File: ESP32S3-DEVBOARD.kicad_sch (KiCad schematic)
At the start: 0 parts

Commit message: Created library for USB_C, ESP32, AND CP2102N, starded to draw schematic
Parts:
- added C1: 100n, symbol Device:C_Small
- added J1: G-Switch_GT-USB-7010ASV, ESP32S3-DEVBOARD:USB_C_Receptacle_G-Switch_GT-USB-7010ASV, symbol ESP32S3-DEVBOARD:USB_C_Receptacle_G-Switch_GT-USB-7010ASV
- added R1, R2: 5k1, symbol Device:R_Small
- added U1: ESP32-S3-WROOM-1, ESP32S3-DEVBOARD:ESP32-S3-WROOM-1, symbol ESP32S3-DEVBOARD:ESP32-S3-WROOM-1
- added U2: CP2102N-A02-GQFN28R, ESP32S3-DEVBOARD:CP2102N-A02-GQFN28R, symbol ESP32S3-DEVBOARD:CP2102N-A02-GQFN28R
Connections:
- new net: U2.29 (GND), U2.3 (GND)
- new net: U1.1 (GND), U1.40 (GND), U1.41 (GND)
- new net +5V: C1.1, J1.A4 (VBUS), J1.A9 (VBUS), J1.B4 (VBUS), J1.B9 (VBUS)
- new net CC1: J1.A5 (CC1), R1.1
- new net CC2: J1.B5 (CC2), R2.1
- new net D_N: J1.A6 (D+), J1.B6 (D+), U2.5 (D-)
- new net D_P: J1.A7 (D-), J1.B7 (D-), U2.4 (D+)
- new net GND: C1.2, J1.A1 (GND), J1.A12 (GND), J1.B1 (GND), J1.B12 (GND), J1.S1 (SHIELD), R1.2, R2.2
- no-connect marks 0 -> 2

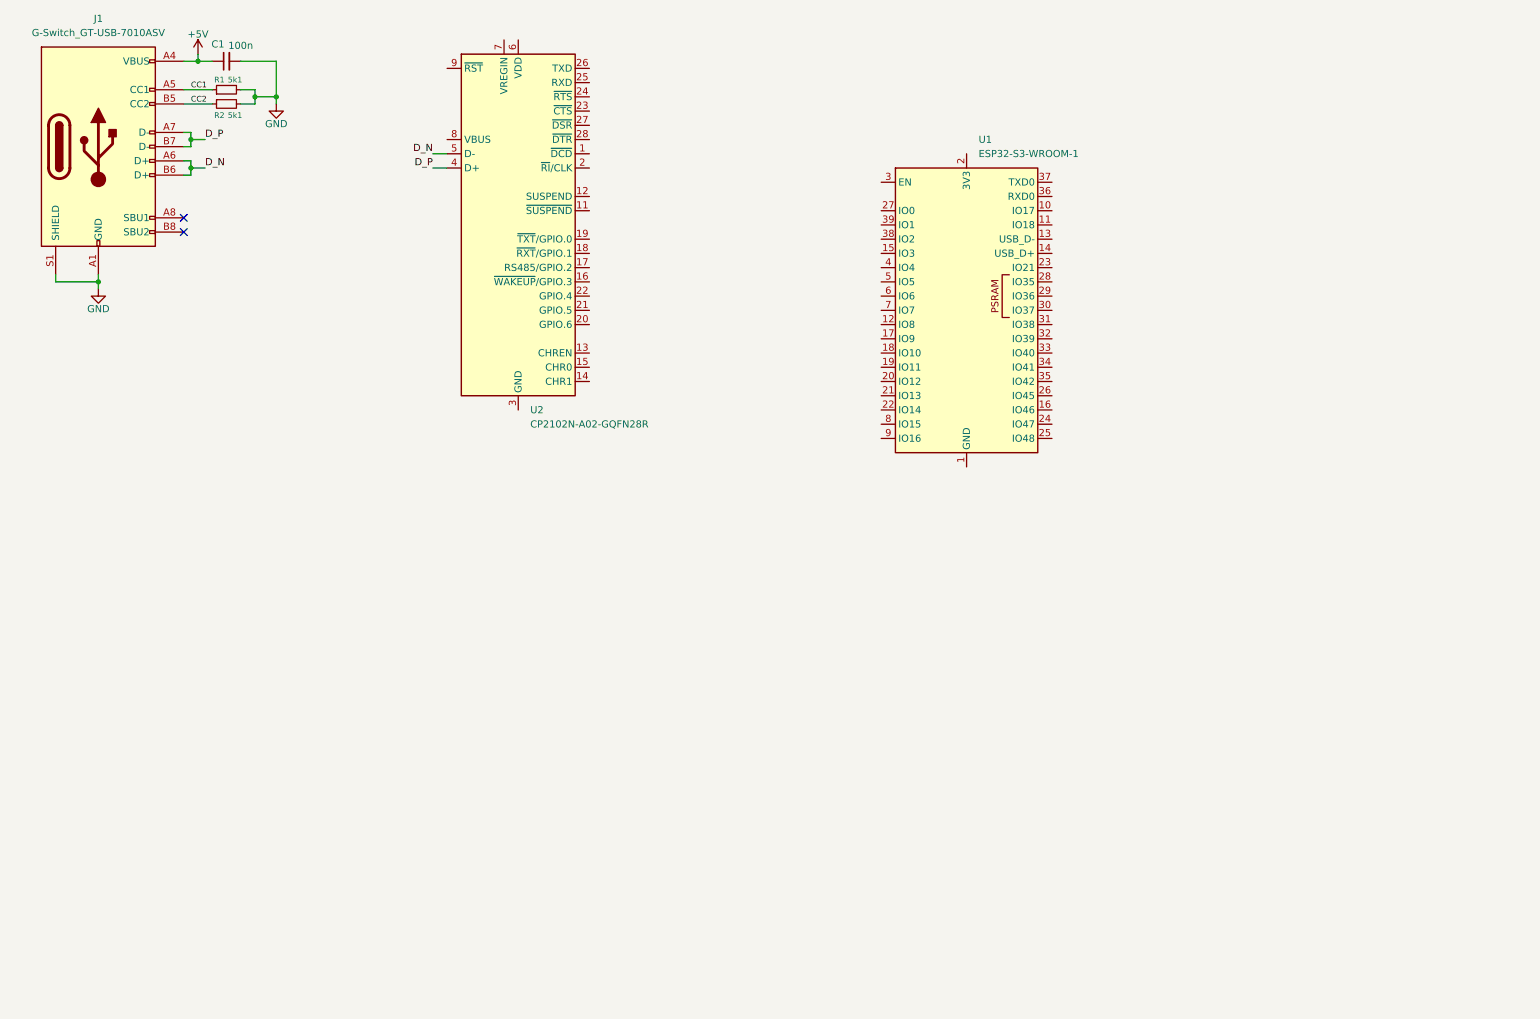
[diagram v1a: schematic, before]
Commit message: Add goldpin, add LDO
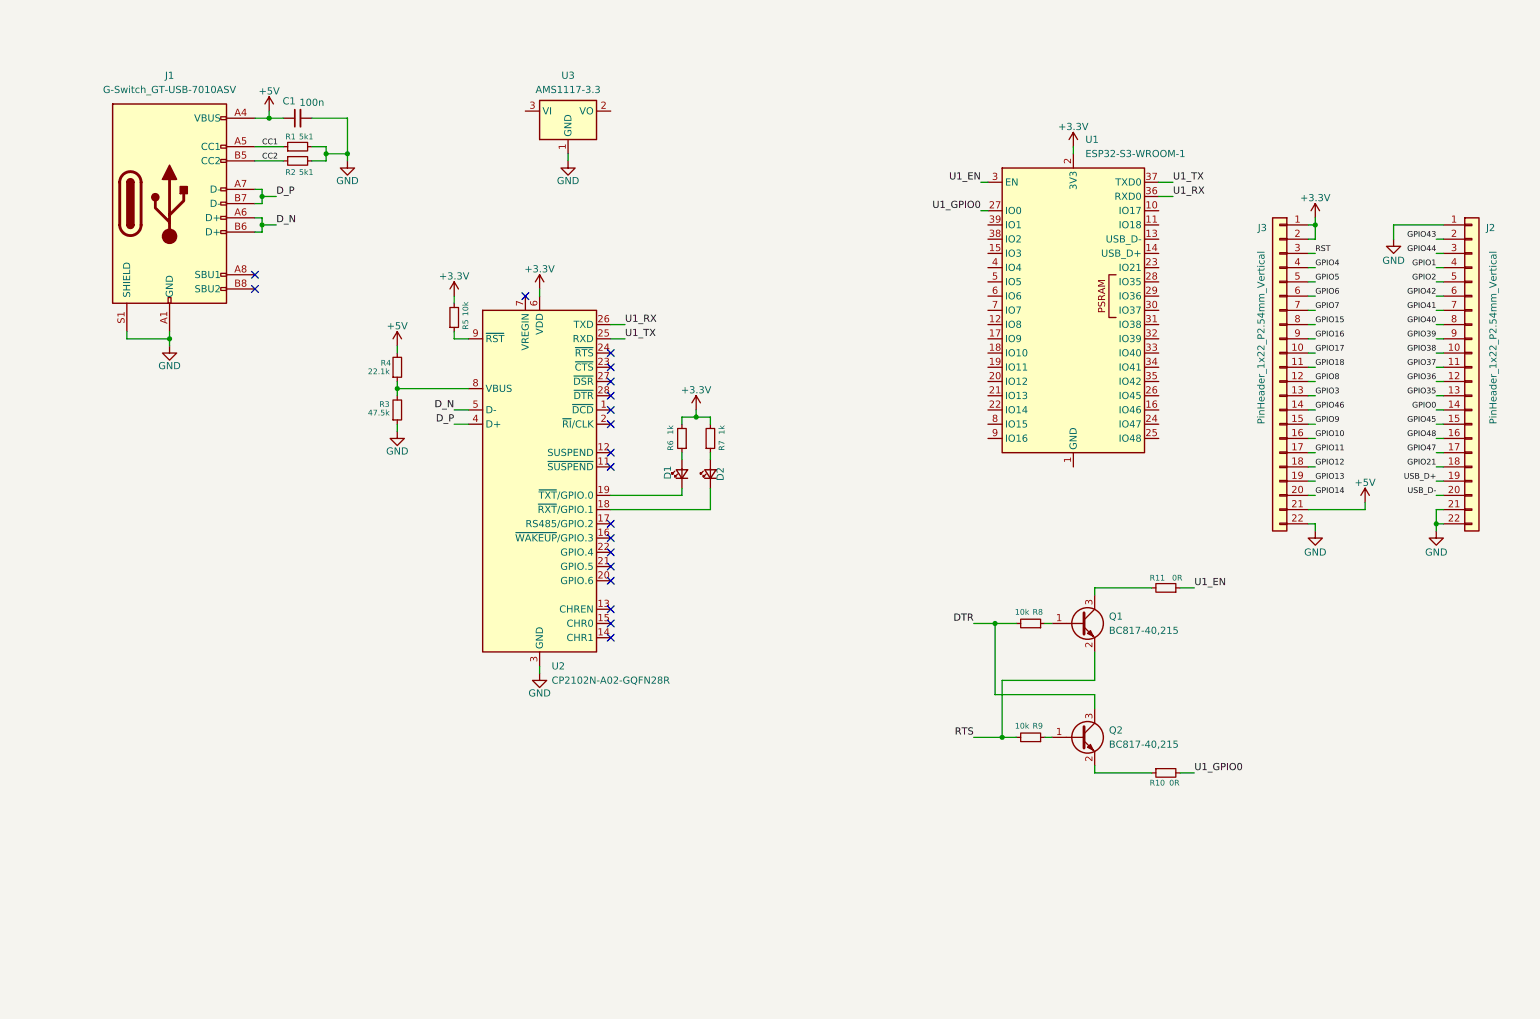
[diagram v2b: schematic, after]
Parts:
- added D1, D2: LED_Small, symbol Device:LED_Small
- added J2, J3: PinHeader_1x22_P2.54mm_Vertical, ESP32S3-DEVBOARD:PinHeader_1x22_P2.54mm_Vertical, symbol ESP32S3-DEVBOARD:PinHeader_1x22_P2.54mm_Vertical
- added Q1, Q2: BC817-40,215, ESP32S3-DEVBOARD:BC817-40,215, symbol ESP32S3-DEVBOARD:BC817-40,215
- added R10, R11: 0R, symbol Device:R_Small
- added R3: 47.5k, symbol Device:R_Small
- added R4: 22.1k, symbol Device:R_Small
- added R5, R8, R9: 10k, symbol Device:R_Small
- added R6, R7: 1k, symbol Device:R_Small
- added U3: AMS1117-3.3, ESP32S3-DEVBOARD:AMS1117-3.3, symbol ESP32S3-DEVBOARD:AMS1117-3.3
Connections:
- net +5V: now also J3.21 (Pin_21), R4.2
- net GND: now also U2.29 (GND), U2.3 (GND), J2.1 (Pin_1), J2.21 (Pin_21), J2.22 (Pin_22), J3.22 (Pin_22), R3.1, U3.1 (GND)
- net at U2.18 (~{RXT}/GPIO.1): now also D2.1 (K)
- net at U2.19 (~{TXT}/GPIO.0): now also D1.1 (K)
- net U1_TX: now reaches U2.25 (RXD)
- net U1_TX: now also U1.37 (TXD0)
- net U1_RX: now reaches U2.26 (TXD)
- net U1_RX: now also U1.36 (RXD0)
- net +3.3V: now reaches U2.6 (VDD)
- net +3.3V: now also U1.2 (3V3), J3.1 (Pin_1), J3.2 (Pin_2), R5.2, R6.2, R7.2
- net at U2.8 (VBUS): now also R3.2, R4.1
- net at U2.9 (~{RST}): now also R5.1
- net U1_GPIO0: now reaches U1.27 (IO0)
- net U1_GPIO0: now also R10.2
- net U1_EN: now reaches U1.3 (EN)
- net U1_EN: now also R11.1
- new net: Q1.1 (B), R8.1
- new net: Q1.3 (C), R11.2
- new net: D1.2 (A), R6.1
- new net: Q2.2 (E), R10.1
- new net: D2.2 (A), R7.1
- new net: Q2.1 (B), R9.1
- new net DTR: Q2.3 (C), R8.2
- new net GPIO0: J2.14 (Pin_14)
- new net GPIO1: J2.4 (Pin_4)
- new net GPIO10: J3.16 (Pin_16)
- new net GPIO11: J3.17 (Pin_17)
- new net GPIO12: J3.18 (Pin_18)
- new net GPIO13: J3.19 (Pin_19)
- new net GPIO14: J3.20 (Pin_20)
- new net GPIO15: J3.8 (Pin_8)
- new net GPIO16: J3.9 (Pin_9)
- new net GPIO17: J3.10 (Pin_10)
- new net GPIO18: J3.11 (Pin_11)
- new net GPIO2: J2.5 (Pin_5)
- new net GPIO21: J2.18 (Pin_18)
- new net GPIO3: J3.13 (Pin_13)
- new net GPIO35: J2.13 (Pin_13)
- new net GPIO36: J2.12 (Pin_12)
- new net GPIO37: J2.11 (Pin_11)
- new net GPIO38: J2.10 (Pin_10)
- new net GPIO39: J2.9 (Pin_9)
- new net GPIO4: J3.4 (Pin_4)
- new net GPIO40: J2.8 (Pin_8)
- new net GPIO41: J2.7 (Pin_7)
- new net GPIO42: J2.6 (Pin_6)
- new net GPIO43: J2.2 (Pin_2)
- new net GPIO44: J2.3 (Pin_3)
- new net GPIO45: J2.15 (Pin_15)
- new net GPIO46: J3.14 (Pin_14)
- new net GPIO47: J2.17 (Pin_17)
- new net GPIO48: J2.16 (Pin_16)
- new net GPIO5: J3.5 (Pin_5)
- new net GPIO6: J3.6 (Pin_6)
- new net GPIO7: J3.7 (Pin_7)
- new net GPIO8: J3.12 (Pin_12)
- new net GPIO9: J3.15 (Pin_15)
- new net RST: J3.3 (Pin_3)
- new net RTS: Q1.2 (E), R9.2
- new net USB_D+: J2.19 (Pin_19)
- new net USB_D-: J2.20 (Pin_20)
- no-connect marks 2 -> 19
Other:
- moved on the sheet: C1, J1, R1, R2, U1, U2

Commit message: Add decoupling capacitors
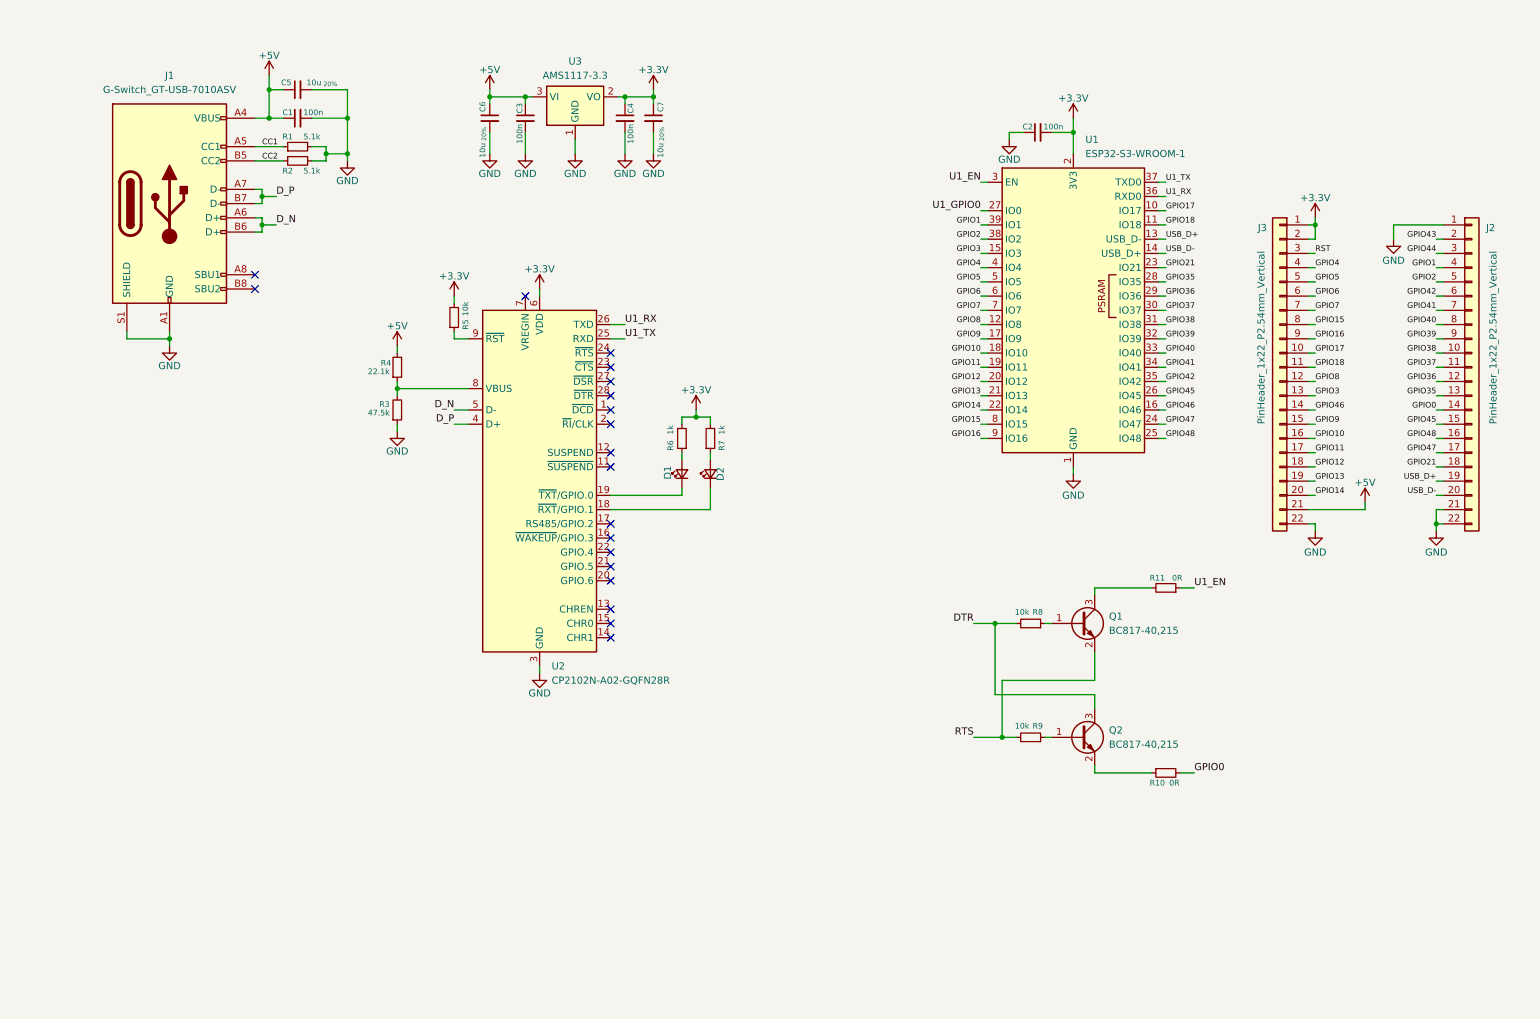
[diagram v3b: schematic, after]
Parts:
- removed C1: 100n, symbol Device:C_Small
- removed R1, R2: 5k1, symbol Device:R_Small
- added C1, C2, C3, C4: 100n, ESP32S3-DEVBOARD:C_0402_1005Metric, symbol ESP32S3-DEVBOARD:CL05B104KO5NNNC
- added C5, C6, C7: 10u_{ 20%}, ESP32S3-DEVBOARD:C_0603_1608Metric, symbol ESP32S3-DEVBOARD:CL10A106MA8NRNC
- added R1, R2: 5.1k, ESP32S3-DEVBOARD:R_0402_1005Metric, symbol ESP32S3-DEVBOARD:0402WGF5101TCE
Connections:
- net +3.3V: now also U3.2 (VO), C2.2, C4.1, C7.1
- net +5V: now also U3.3 (VI), C1.1, C3.1, C5.1, C6.1
- net CC1: now also R1.1
- net CC2: now also R2.1
- net GND: now also U1.1 (GND), U1.40 (GND), U1.41 (GND), C1.2, C2.1, C3.2, C4.2, C5.2, C6.2, C7.2, R1.2, R2.2
- net GPIO0: now also R10.2
- net GPIO1: now also U1.39 (IO1)
- net GPIO10: now also U1.18 (IO10)
- net GPIO11: now also U1.19 (IO11)
- net GPIO12: now also U1.20 (IO12)
- net GPIO13: now also U1.21 (IO13)
- net GPIO14: now also U1.22 (IO14)
- net GPIO15: now also U1.8 (IO15)
- net GPIO16: now also U1.9 (IO16)
- net GPIO17: now also U1.10 (IO17)
- net GPIO18: now also U1.11 (IO18)
- net GPIO2: now also U1.38 (IO2)
- net GPIO21: now also U1.23 (IO21)
- net GPIO3: now also U1.15 (IO3)
- net GPIO35: now also U1.28 (IO35)
- net GPIO36: now also U1.29 (IO36)
- net GPIO37: now also U1.30 (IO37)
- net GPIO38: now also U1.31 (IO38)
- net GPIO39: now also U1.32 (IO39)
- net GPIO4: now also U1.4 (IO4)
- net GPIO40: now also U1.33 (IO40)
- net GPIO41: now also U1.34 (IO41)
- net GPIO42: now also U1.35 (IO42)
- net GPIO45: now also U1.26 (IO45)
- net GPIO46: now also U1.16 (IO46)
- net GPIO47: now also U1.24 (IO47)
- net GPIO48: now also U1.25 (IO48)
- net GPIO5: now also U1.5 (IO5)
- net GPIO6: now also U1.6 (IO6)
- net GPIO7: now also U1.7 (IO7)
- net GPIO8: now also U1.12 (IO8)
- net GPIO9: now also U1.17 (IO9)
- net U1_GPIO0: no longer R10.2
- net USB_D+: now also U1.13 (USB_D-)
- net USB_D-: now also U1.14 (USB_D+)
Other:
- moved on the sheet: U3

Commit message: Add two resisotrs to library
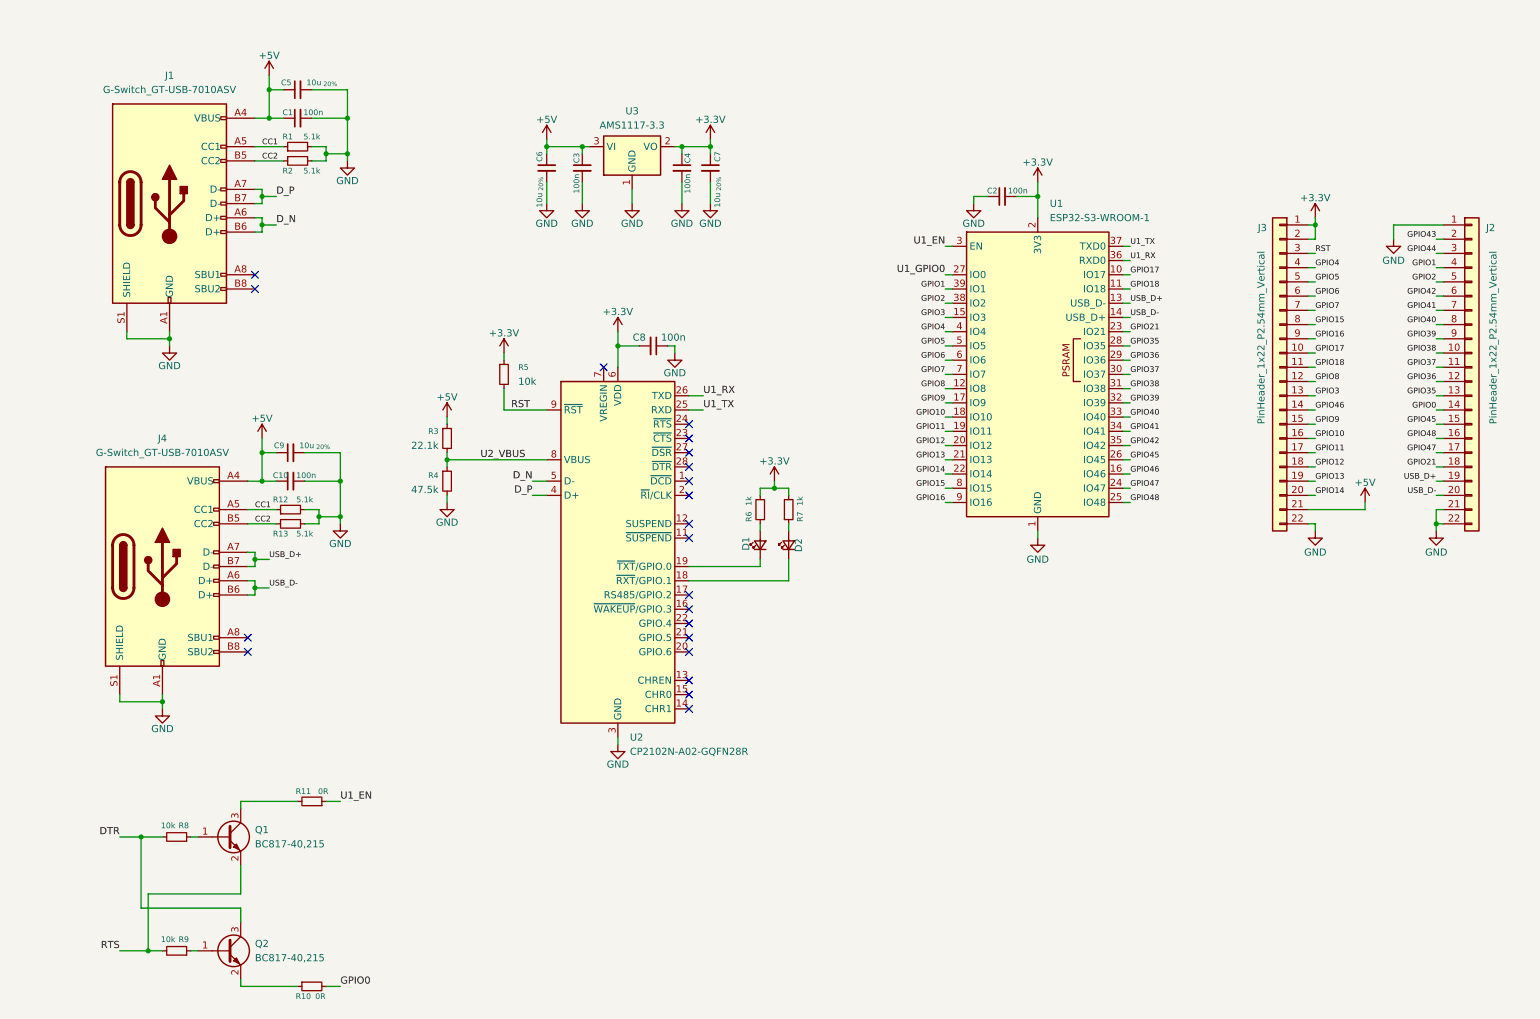
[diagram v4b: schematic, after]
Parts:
- removed R3: 47.5k, symbol Device:R_Small
- removed R4: 22.1k, symbol Device:R_Small
- removed R5, R8: 10k, symbol Device:R_Small
- added C10, C8: 100n, ESP32S3-DEVBOARD:C_0402_1005Metric, symbol ESP32S3-DEVBOARD:CL05B104KO5NNNC
- added C9: 10u_{ 20%}, ESP32S3-DEVBOARD:C_0603_1608Metric, symbol ESP32S3-DEVBOARD:CL10A106MA8NRNC
- added J4: G-Switch_GT-USB-7010ASV, ESP32S3-DEVBOARD:USB_C_Receptacle_G-Switch_GT-USB-7010ASV, symbol ESP32S3-DEVBOARD:USB_C_Receptacle_G-Switch_GT-USB-7010ASV
- added R12, R13: 5.1k, ESP32S3-DEVBOARD:R_0402_1005Metric, symbol ESP32S3-DEVBOARD:0402WGF5101TCE
- added R3: 22.1k, ESP32S3-DEVBOARD:R_0402_1005Metric, symbol ESP32S3-DEVBOARD:FRC0402F2212TS
- added R4: 47.5k, ESP32S3-DEVBOARD:R_0402_1005Metric, symbol ESP32S3-DEVBOARD:0402WGF4752TCE
- added R5, R8: 10k, ESP32S3-DEVBOARD:R_0402_1005Metric, symbol ESP32S3-DEVBOARD:RC0402FR-0710KL
- R9: footprint (none) -> ESP32S3-DEVBOARD:R_0402_1005Metric; symbol Device:R_Small -> ESP32S3-DEVBOARD:RC0402FR-0710KL; LCSC (none) -> C60490; Mfr. Part #  (none) -> RC0402FR-0710KL
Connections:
- net +3.3V: now also C8.2, R5.1
- net +5V: now also C10.1, C9.1, J4.A4 (VBUS), J4.A9 (VBUS), J4.B4 (VBUS), J4.B9 (VBUS), R3.1
- net CC1: now also J4.A5 (CC1), R12.1
- net CC2: now also J4.B5 (CC2), R13.1
- net DTR: now also R8.2
- net GND: now also C10.2, C8.1, C9.2, J4.A1 (GND), J4.A12 (GND), J4.B1 (GND), J4.B12 (GND), J4.S1 (SHIELD), R12.2, R13.2, R4.2
- net RST: now also U2.9 (~{RST}), R5.2
- net USB_D+: now also J4.A7 (D-), J4.B7 (D-)
- net USB_D-: now also J4.A6 (D+), J4.B6 (D+)
- net at Q1.1 (B): now also R8.1
- net U2_VBUS: now reaches U2.8 (VBUS)
- net U2_VBUS: now also R3.2, R4.1
- no-connect marks 19 -> 21
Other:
- moved on the sheet: C2, C3, C4, C6, C7, D1, D2, Q1, Q2, R10, R11, R6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
